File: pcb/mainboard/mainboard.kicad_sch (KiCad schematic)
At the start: 0 parts

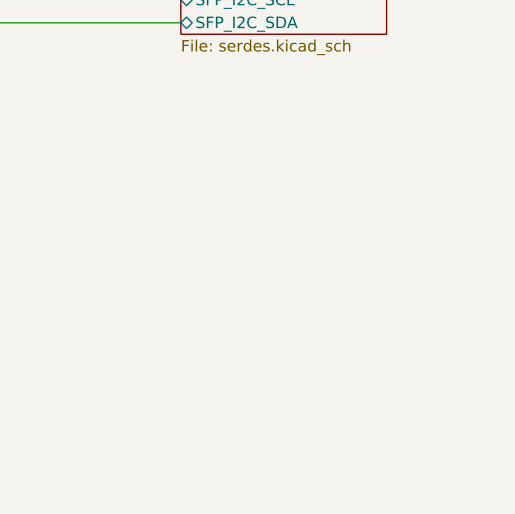
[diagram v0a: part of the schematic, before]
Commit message: Initial floorplanning work, added SFP+ LEDs
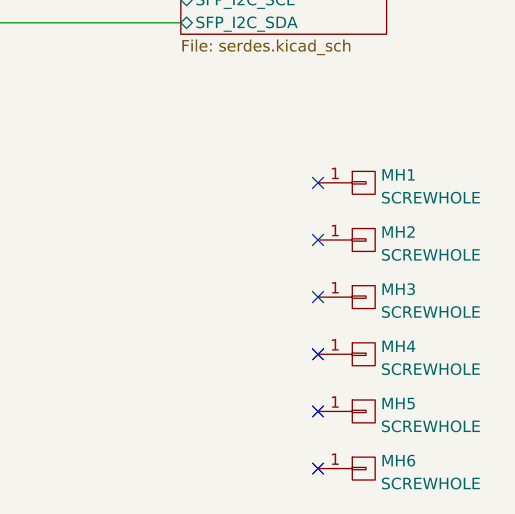
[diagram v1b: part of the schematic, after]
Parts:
- added MH1, MH2, MH3, MH4, MH5, MH6: SCREWHOLE, azonenberg_pcb:MECHANICAL_CLEARANCEHOLE_4_40, symbol conn:CONN_01X01
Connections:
- no-connect marks 0 -> 6
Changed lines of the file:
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@@
   (junction (at 92.71 31.75) (diameter 0) (color 0 0 0 0)
   )
+  (no_connect (at 222.25 157.48))
+  (no_connect (at 222.25 132.08))
+  (no_connect (at 222.25 144.78))
+  (no_connect (at 222.25 138.43))
+  (no_connect (at 222.25 151.13))
+  (no_connect (at 222.25 125.73))
   (wire (pts (xy 85.09 107.95) (xy 93.98 107.95))
     (stroke (width 0) (type default) (color 0 0 0 0))
@@
   (label "MCU_READY" (at 43.18 39.37 180)
     (effects (font (size 1.27 1.27)) (justify right bottom))
+  )
+  (symbol (lib_id "conn:CONN_01X01") (at 227.33 151.13 0) (unit 1)
+    (in_bom yes) (on_board yes) (fields_autoplaced)
+    (property "Reference" "MH5" (id 0) (at 229.235 150.2953 0)
+      (effects (font (size 1.27 1.27)) (justify left))
+    )
+    (property "Value" "SCREWHOLE" (id 1) (at 229.235 152.8322 0)
+      (effects (font (size 1.27 1.27)) (justify left))
+    )
+    (property "Footprint" "azonenberg_pcb:MECHANICAL_CLEARANCEHOLE_4_40" (id 2) (at 227.33 151.13 0)
+      (effects (font (size 1.27 1.27)) hide)
+    )
+    (property "Datasheet" "" (id 3) (at 227.33 151.13 0)
+      (effects (font (size 1.27 1.27)) hide)
+    )
+    (pin "1")
+  )
+  (symbol (lib_id "conn:CONN_01X01") (at 227.33 157.48 0) (unit 1)
+    (in_bom yes) (on_board yes) (fields_autoplaced)
+    (property "Reference" "MH6" (id 0) (at 229.235 156.6453 0)
+      (effects (font (size 1.27 1.27)) (justify left))
+    )
+    (property "Value" "SCREWHOLE" (id 1) (at 229.235 159.1822 0)
+      (effects (font (size 1.27 1.27)) (justify left))
+    )
+    (property "Footprint" "azonenberg_pcb:MECHANICAL_CLEARANCEHOLE_4_40" (id 2) (at 227.33 157.48 0)
+      (effects (font (size 1.27 1.27)) hide)
+    )
+    (property "Datasheet" "" (id 3) (at 227.33 157.48 0)
+      (effects (font (size 1.27 1.27)) hide)
+    )
+    (pin "1")
+  )
+  (symbol (lib_id "conn:CONN_01X01") (at 227.33 144.78 0) (unit 1)
+    (in_bom yes) (on_board yes) (fields_autoplaced)
+    (property "Reference" "MH4" (id 0) (at 229.235 143.9453 0)
+      (effects (font (size 1.27 1.27)) (justify left))
+    )
+    (property "Value" "SCREWHOLE" (id 1) (at 229.235 146.4822 0)
+      (effects (font (size 1.27 1.27)) (justify left))
+    )
+    (property "Footprint" "azonenberg_pcb:MECHANICAL_CLEARANCEHOLE_4_40" (id 2) (at 227.33 144.78 0)
+      (effects (font (size 1.27 1.27)) hide)
+    )
+    (property "Datasheet" "" (id 3) (at 227.33 144.78 0)
+      (effects (font (size 1.27 1.27)) hide)
+    )
+    (pin "1")
+  )
+  (symbol (lib_id "conn:CONN_01X01") (at 227.33 138.43 0) (unit 1)
+    (in_bom yes) (on_board yes) (fields_autoplaced)
+    (property "Reference" "MH3" (id 0) (at 229.235 137.5953 0)
+      (effects (font (size 1.27 1.27)) (justify left))
+    )
+    (property "Value" "SCREWHOLE" (id 1) (at 229.235 140.1322 0)
+      (effects (font (size 1.27 1.27)) (justify left))
+    )
+    (property "Footprint" "azonenberg_pcb:MECHANICAL_CLEARANCEHOLE_4_40" (id 2) (at 227.33 138.43 0)
+      (effects (font (size 1.27 1.27)) hide)
+    )
+    (property "Datasheet" "" (id 3) (at 227.33 138.43 0)
+      (effects (font (size 1.27 1.27)) hide)
+    )
+    (pin "1")
+  )
+  (symbol (lib_id "conn:CONN_01X01") (at 227.33 132.08 0) (unit 1)
+    (in_bom yes) (on_board yes) (fields_autoplaced)
+    (property "Reference" "MH2" (id 0) (at 229.235 131.2453 0)
+      (effects (font (size 1.27 1.27)) (justify left))
+    )
+    (property "Value" "SCREWHOLE" (id 1) (at 229.235 133.7822 0)
+      (effects (font (size 1.27 1.27)) (justify left))
+    )
+    (property "Footprint" "azonenberg_pcb:MECHANICAL_CLEARANCEHOLE_4_40" (id 2) (at 227.33 132.08 0)
+      (effects (font (size 1.27 1.27)) hide)
+    )
+    (property "Datasheet" "" (id 3) (at 227.33 132.08 0)
+      (effects (font (size 1.27 1.27)) hide)
+    )
+    (pin "1")
+  )
+  (symbol (lib_id "conn:CONN_01X01") (at 227.33 125.73 0) (unit 1)
+    (in_bom yes) (on_board yes) (fields_autoplaced)
+    (property "Reference" "MH1" (id 0) (at 229.235 124.8953 0)
+      (effects (font (size 1.27 1.27)) (justify left))
+    )
+    (property "Value" "SCREWHOLE" (id 1) (at 229.235 127.4322 0)
+      (effects (font (size 1.27 1.27)) (justify left))
+    )
+    (property "Footprint" "azonenberg_pcb:MECHANICAL_CLEARANCEHOLE_4_40" (id 2) (at 227.33 125.73 0)
+      (effects (font (size 1.27 1.27)) hide)
+    )
+    (property "Datasheet" "" (id 3) (at 227.33 125.73 0)
+      (effects (font (size 1.27 1.27)) hide)
+    )
+    (pin "1")
   )
   (sheet (at 152.4 24.13) (size 17.78 7.62) (fields_autoplaced)
@@
       (reference "D38") (unit 1) (value "SZESD7471N2T5G") (footprint "azonenberg_pcb:SOD882")
     )
+    (path "/21b6a12b-d0d3-486b-ae28-812475c71b31/7ff868be-bb29-43c6-a7cf-c687254ab7b8"
+      (reference "D39") (unit 1) (value "GREEN") (footprint "azonenberg_pcb:EIA_0603_LED")
+    )
+    (path "/21b6a12b-d0d3-486b-ae28-812475c71b31/ff18065c-db69-45d8-9fd3-243515792a3d"
+      (reference "D40") (unit 1) (value "GREEN") (footprint "azonenberg_pcb:EIA_0603_LED")
+    )
     (path "/3921899c-e822-4b0b-b0c1-b63fbde0e17d/7fbfb59d-1b4d-4a26-b85c-8624d3f1d20d"
       (reference "F1") (unit 1) (value "2A") (footprint "azonenberg_pcb:EIA_0603_CAP_NOSILK")
@@
       (reference "M1") (unit 1) (value "960-23-23-F-AB-0") (footprint "azonenberg_pcb:HEATSINK_WAKEFIELDVETTE_960-23-23-F-AB-0")
     )
+    (path "/eb063380-1a9b-4dc0-8558-af6481d57a5e"
+      (reference "MH1") (unit 1) (value "SCREWHOLE") (footprint "azonenberg_pcb:MECHANICAL_CLEARANCEHOLE_4_40")
+    )
+    (path "/8ab51005-c859-4032-bc04-63454a26aa7d"
+      (reference "MH2") (unit 1) (value "SCREWHOLE") (footprint "azonenberg_pcb:MECHANICAL_CLEARANCEHOLE_4_40")
+    )
+    (path "/5300d5b9-daa4-4bf8-9b23-3ab0c84377d0"
+      (reference "MH3") (unit 1) (value "SCREWHOLE") (footprint "azonenberg_pcb:MECHANICAL_CLEARANCEHOLE_4_40")
+    )
+    (path "/45dfa19c-258d-48e8-8c3c-cd78505bedf8"
+      (reference "MH4") (unit 1) (value "SCREWHOLE") (footprint "azonenberg_pcb:MECHANICAL_CLEARANCEHOLE_4_40")
+    )
+    (path "/30466c8d-9c49-4e46-adbd-828e402017cf"
+      (reference "MH5") (unit 1) (value "SCREWHOLE") (footprint "azonenberg_pcb:MECHANICAL_CLEARANCEHOLE_4_40")
+    )
+    (path "/3c71215e-8f0d-48f0-aa63-951e4159d056"
+      (reference "MH6") (unit 1) (value "SCREWHOLE") (footprint "azonenberg_pcb:MECHANICAL_CLEARANCEHOLE_4_40")
+    )
     (path "/3921899c-e822-4b0b-b0c1-b63fbde0e17d/66f6e42c-ea1b-4ca3-a55d-ec886e6013f2"
       (reference "R1") (unit 1) (value "10K") (footprint "azonenberg_pcb:EIA_0402_RES_NOSILK")
@@
       (reference "R162") (unit 1) (value "1K") (footprint "azonenberg_pcb:EIA_0402_RES_NOSILK")
     )
+    (path "/21b6a12b-d0d3-486b-ae28-812475c71b31/9964f173-69c3-4e6b-a921-d0aa42a67802"
+      (reference "R163") (unit 1) (value "470") (footprint "azonenberg_pcb:EIA_0402_RES_NOSILK")
+    )
+    (path "/21b6a12b-d0d3-486b-ae28-812475c71b31/dc6f007a-a37c-4997-a685-30aaac37f23a"
+      (reference "R164") (unit 1) (value "470") (footprint "azonenberg_pcb:EIA_0402_RES_NOSILK")
+    )
     (path "/3921899c-e822-4b0b-b0c1-b63fbde0e17d/248d615a-45d4-49c6-ba6d-b7d7f1fc7357"

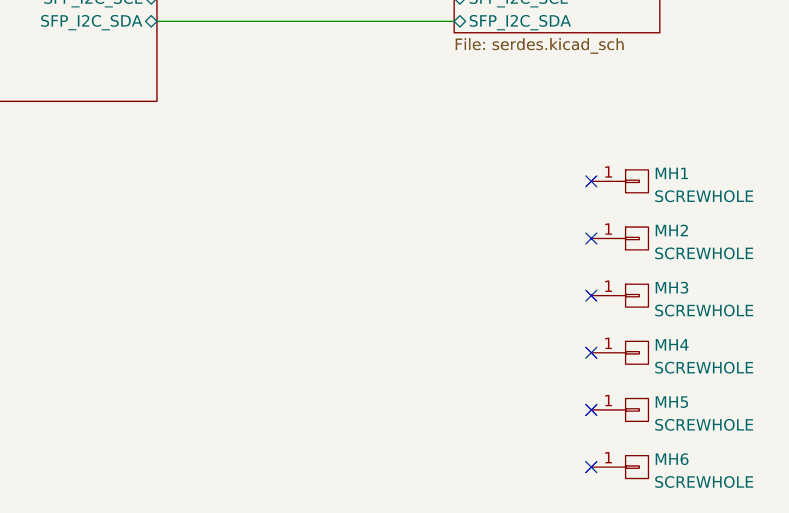
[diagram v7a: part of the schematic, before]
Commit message: Finished first pass of routing cleanup, moved FPGA JTAG to edge of board
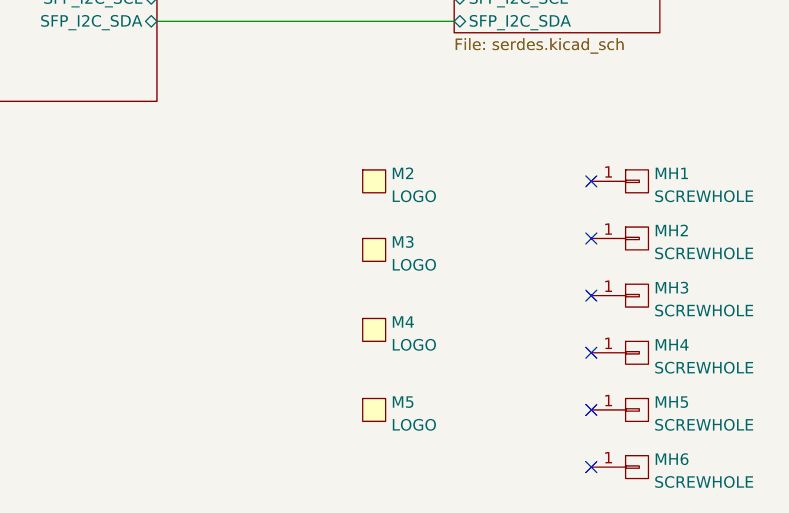
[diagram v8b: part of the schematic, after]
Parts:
- added M2: LOGO, azonenberg_pcb:LONGTHING-1200DPI, symbol special-azonenberg:MECHANICAL
- added M3: LOGO, w_logo:Logo_silk_ROHS_5x2.8mm, symbol special-azonenberg:MECHANICAL
- added M4: LOGO, w_logo:Logo_silk_OSHW_6x6mm, symbol special-azonenberg:MECHANICAL
- added M5: LOGO, w_logo:Logo_silk_WEEE_3.4x5mm, symbol special-azonenberg:MECHANICAL
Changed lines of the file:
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@@
   (title_block
     (title "Trigger Crossbar")
-    (date "2023-12-25")
+    (date "2023-12-26")
     (rev "0.1")
     (company "Antikernel Labs")
@@
     (effects (font (size 1.27 1.27)) (justify right bottom))
   )
+  (symbol (lib_id "special-azonenberg:MECHANICAL") (at 196.85 133.35 0) (unit 1)
+    (in_bom yes) (on_board yes) (fields_autoplaced)
+    (property "Reference" "M3" (id 0) (at 200.025 132.5153 0)
+      (effects (font (size 1.27 1.27)) (justify left))
+    )
+    (property "Value" "LOGO" (id 1) (at 200.025 135.0522 0)
+      (effects (font (size 1.27 1.27)) (justify left))
+    )
+    (property "Footprint" "w_logo:Logo_silk_ROHS_5x2.8mm" (id 2) (at 196.85 133.35 0)
+      (effects (font (size 1.27 1.27)) hide)
+    )
+    (property "Datasheet" "" (id 3) (at 196.85 133.35 0)
+      (effects (font (size 1.27 1.27)) hide)
+    )
+  )
+  (symbol (lib_id "special-azonenberg:MECHANICAL") (at 196.85 151.13 0) (unit 1)
+    (in_bom yes) (on_board yes) (fields_autoplaced)
+    (property "Reference" "M5" (id 0) (at 200.025 150.2953 0)
+      (effects (font (size 1.27 1.27)) (justify left))
+    )
+    (property "Value" "LOGO" (id 1) (at 200.025 152.8322 0)
+      (effects (font (size 1.27 1.27)) (justify left))
+    )
+    (property "Footprint" "w_logo:Logo_silk_WEEE_3.4x5mm" (id 2) (at 196.85 151.13 0)
+      (effects (font (size 1.27 1.27)) hide)
+    )
+    (property "Datasheet" "" (id 3) (at 196.85 151.13 0)
+      (effects (font (size 1.27 1.27)) hide)
+    )
+  )
   (symbol (lib_id "conn:CONN_01X01") (at 227.33 151.13 0) (unit 1)
     (in_bom yes) (on_board yes) (fields_autoplaced)
@@
     )
     (pin "1")
+  )
+  (symbol (lib_id "special-azonenberg:MECHANICAL") (at 196.85 142.24 0) (unit 1)
+    (in_bom yes) (on_board yes) (fields_autoplaced)
+    (property "Reference" "M4" (id 0) (at 200.025 141.4053 0)
+      (effects (font (size 1.27 1.27)) (justify left))
+    )
+    (property "Value" "LOGO" (id 1) (at 200.025 143.9422 0)
+      (effects (font (size 1.27 1.27)) (justify left))
+    )
+    (property "Footprint" "w_logo:Logo_silk_OSHW_6x6mm" (id 2) (at 196.85 142.24 0)
+      (effects (font (size 1.27 1.27)) hide)
+    )
+    (property "Datasheet" "" (id 3) (at 196.85 142.24 0)
+      (effects (font (size 1.27 1.27)) hide)
+    )
+  )
+  (symbol (lib_id "special-azonenberg:MECHANICAL") (at 196.85 125.73 0) (unit 1)
+    (in_bom yes) (on_board yes) (fields_autoplaced)
+    (property "Reference" "M2" (id 0) (at 200.025 124.8953 0)
+      (effects (font (size 1.27 1.27)) (justify left))
+    )
+    (property "Value" "LOGO" (id 1) (at 200.025 127.4322 0)
+      (effects (font (size 1.27 1.27)) (justify left))
+    )
+    (property "Footprint" "azonenberg_pcb:LONGTHING-1200DPI" (id 2) (at 196.85 125.73 0)
+      (effects (font (size 1.27 1.27)) hide)
+    )
+    (property "Datasheet" "" (id 3) (at 196.85 125.73 0)
+      (effects (font (size 1.27 1.27)) hide)
+    )
   )
   (symbol (lib_id "conn:CONN_01X01") (at 227.33 125.73 0) (unit 1)
@@
       (reference "M1") (unit 1) (value "960-23-23-F-AB-0") (footprint "azonenberg_pcb:HEATSINK_WAKEFIELDVETTE_960-23-23-F-AB-0")
     )
+    (path "/eaf94b08-7a24-4475-baa4-23b51a719e93"
+      (reference "M2") (unit 1) (value "LOGO") (footprint "azonenberg_pcb:LONGTHING-1200DPI")
+    )
+    (path "/095da2ca-9d51-46ac-b1c0-123b446076e0"
+      (reference "M3") (unit 1) (value "LOGO") (footprint "w_logo:Logo_silk_ROHS_5x2.8mm")
+    )
+    (path "/ea7e5e1a-98c3-4b05-9524-5357ca8298e9"
+      (reference "M4") (unit 1) (value "LOGO") (footprint "w_logo:Logo_silk_OSHW_6x6mm")
+    )
+    (path "/166260ce-ce8c-4b2f-b946-c6f444534a8a"
+      (reference "M5") (unit 1) (value "LOGO") (footprint "w_logo:Logo_silk_WEEE_3.4x5mm")
+    )
     (path "/eb063380-1a9b-4dc0-8558-af6481d57a5e"
